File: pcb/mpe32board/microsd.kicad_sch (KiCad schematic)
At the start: 6 parts, among them J44 Micro_SD_Card

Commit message: layout stuff
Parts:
- J44: footprint (none) -> Connector_Card:microSD_HC_Molex_47219-2001
- R95, R96, R97, R98, R99: footprint (none) -> Resistor_SMD:R_0603_1608Metric
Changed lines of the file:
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@@
 			)
 		)
-		(property "Footprint" ""
+		(property "Footprint" "Resistor_SMD:R_0603_1608Metric"
 			(at 134.62 68.58 0)
 			(effects
@@
 			)
 		)
-		(property "Footprint" ""
+		(property "Footprint" "Resistor_SMD:R_0603_1608Metric"
 			(at 119.38 68.58 0)
 			(effects
@@
 			)
 		)
-		(property "Footprint" ""
+		(property "Footprint" "Connector_Card:microSD_HC_Molex_47219-2001"
 			(at 204.47 76.2 0)
 			(effects
@@
 			)
 		)
-		(property "Footprint" ""
+		(property "Footprint" "Resistor_SMD:R_0603_1608Metric"
 			(at 111.76 68.58 0)
 			(effects
@@
 			)
 		)
-		(property "Footprint" ""
+		(property "Footprint" "Resistor_SMD:R_0603_1608Metric"
 			(at 127 68.58 0)
 			(effects
@@
 			)
 		)
-		(property "Footprint" ""
+		(property "Footprint" "Resistor_SMD:R_0603_1608Metric"
 			(at 142.24 68.58 0)
 			(effects

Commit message: board layout stuff
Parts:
- removed J44: Micro_SD_Card, Connector_Card:microSD_HC_Molex_47219-2001, symbol Connector:Micro_SD_Card
- added J48: Micro_SD_Card_Det_Hirose_DM3AT, Connector_Card:microSD_HC_Hirose_DM3D-SF, symbol Connector:Micro_SD_Card_Det_Hirose_DM3AT
- added U11: IP4252CZ16, Package_SON:Nexperia_HUSON-16_USON-16-1EP_1.35x3.3mm_P0.4mm_EP0.4x2.8mm, symbol Power_Protection:IP4252CZ16
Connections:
- net +3V3: now also J48.4 (VDD)
- net GND: now also J48.11 (SHIELD), J48.6 (VSS), J48.9 (DET_B)
- net SDMMC1_CK: now also U11.6 (CH6)
- net SDMMC1_CMD: now also U11.4 (CH4)
- net SDMMC1_D0: now also U11.7 (CH7)
- net SDMMC1_D1: now also U11.8 (CH8)
- net SDMMC1_D2: now also U11.2 (CH2)
- net SDMMC1_D3: now also U11.3 (CH3)
- new net: J48.7 (DAT0), U11.10 (CH7)
- new net: J48.5 (CLK), U11.11 (CH6)
- new net: J48.3 (CMD), U11.13 (CH4)
- new net: J48.2 (DAT3/CD), U11.14 (CH3)
- new net: J48.1 (DAT2), U11.15 (CH2)
- new net: J48.10 (DET_A), U11.16 (CH1)
- new net: J48.8 (DAT1), U11.9 (CH8)
- new net SDCARD_DET: U11.1 (CH1)
- no-connect marks 0 -> 2
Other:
- note removed: "could use esd protection!!!"
- moved on the sheet: R95, R96, R97, R98, R99

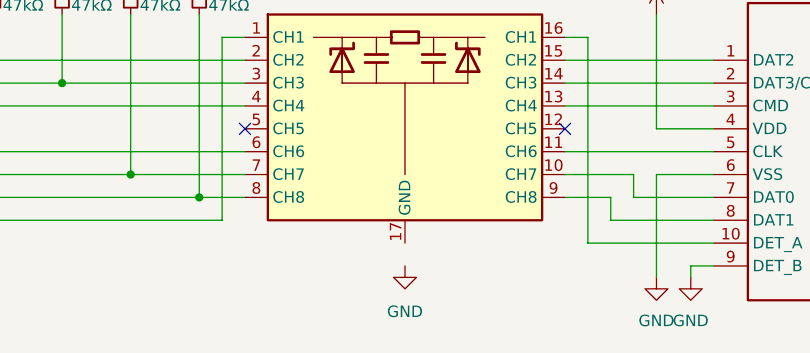
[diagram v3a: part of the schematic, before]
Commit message: routed audio codec and sdram
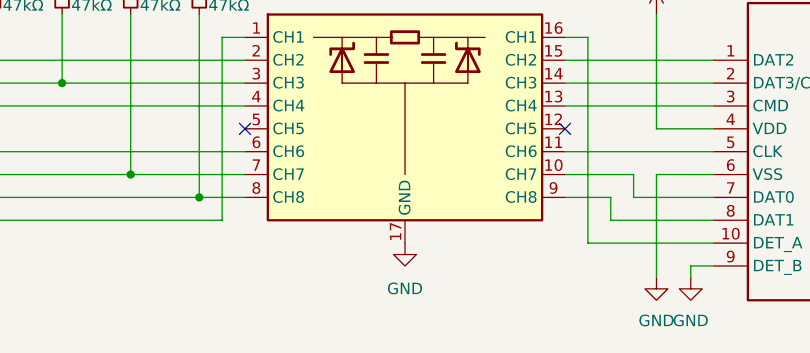
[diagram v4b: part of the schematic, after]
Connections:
- net GND: now also U11.17 (GND)
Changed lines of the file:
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@@
 	(symbol
 		(lib_id "power:GND")
-		(at 140.97 116.84 0)
+		(at 140.97 114.3 0)
 		(unit 1)
 		(body_style 1)
@@
 		(fields_autoplaced yes)
 		(property "Reference" "#PWR0172"
-			(at 140.97 123.19 0)
+			(at 140.97 120.65 0)
 			(hide yes)
 			(show_name no)
@@
 		)
 		(property "Value" "GND"
-			(at 140.97 121.92 0)
+			(at 140.97 119.38 0)
 			(show_name no)
 			(do_not_autoplace no)
@@
 		)
 		(property "Footprint" ""
-			(at 140.97 116.84 0)
+			(at 140.97 114.3 0)
 			(hide yes)
 			(show_name no)
@@
 		)
 		(property "Datasheet" ""
-			(at 140.97 116.84 0)
+			(at 140.97 114.3 0)
 			(hide yes)
 			(show_name no)
@@
 		)
 		(property "Description" "Power symbol creates a global label with name \"GND\" , ground"
-			(at 140.97 116.84 0)
+			(at 140.97 114.3 0)
 			(hide yes)
 			(show_name no)

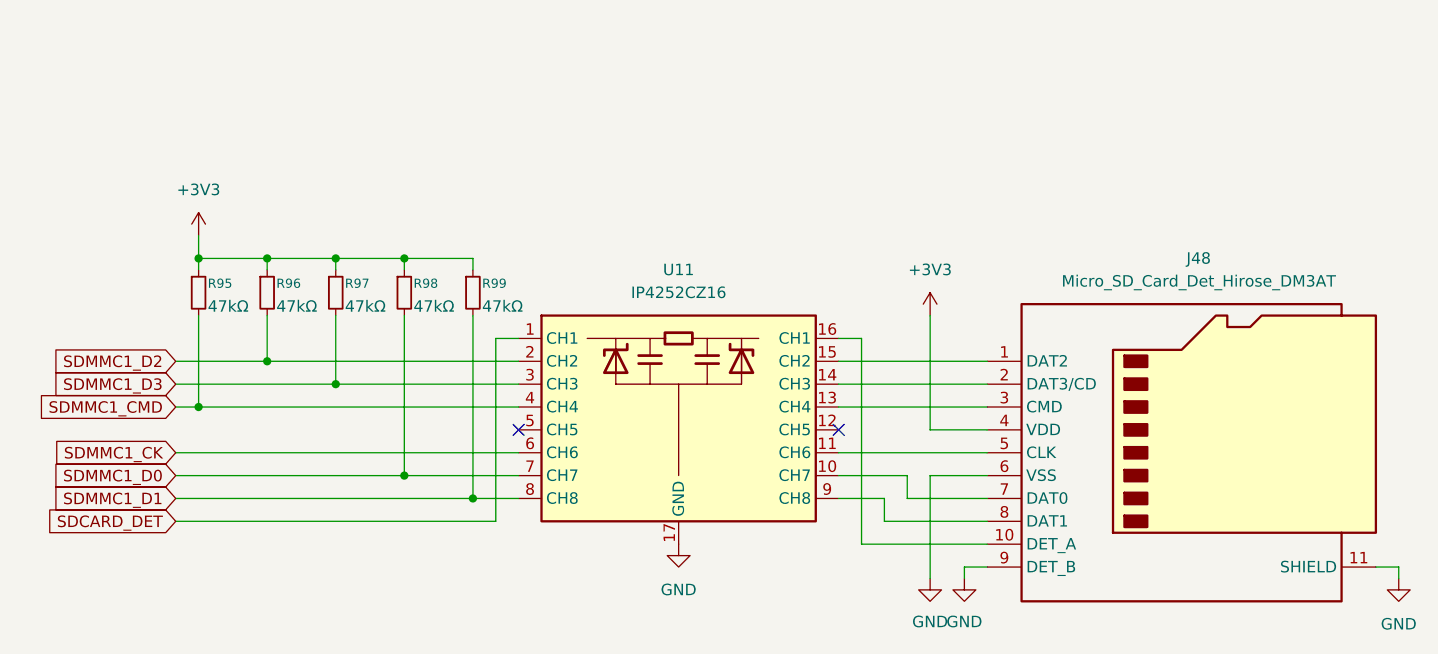
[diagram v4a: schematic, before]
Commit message: length match sdram
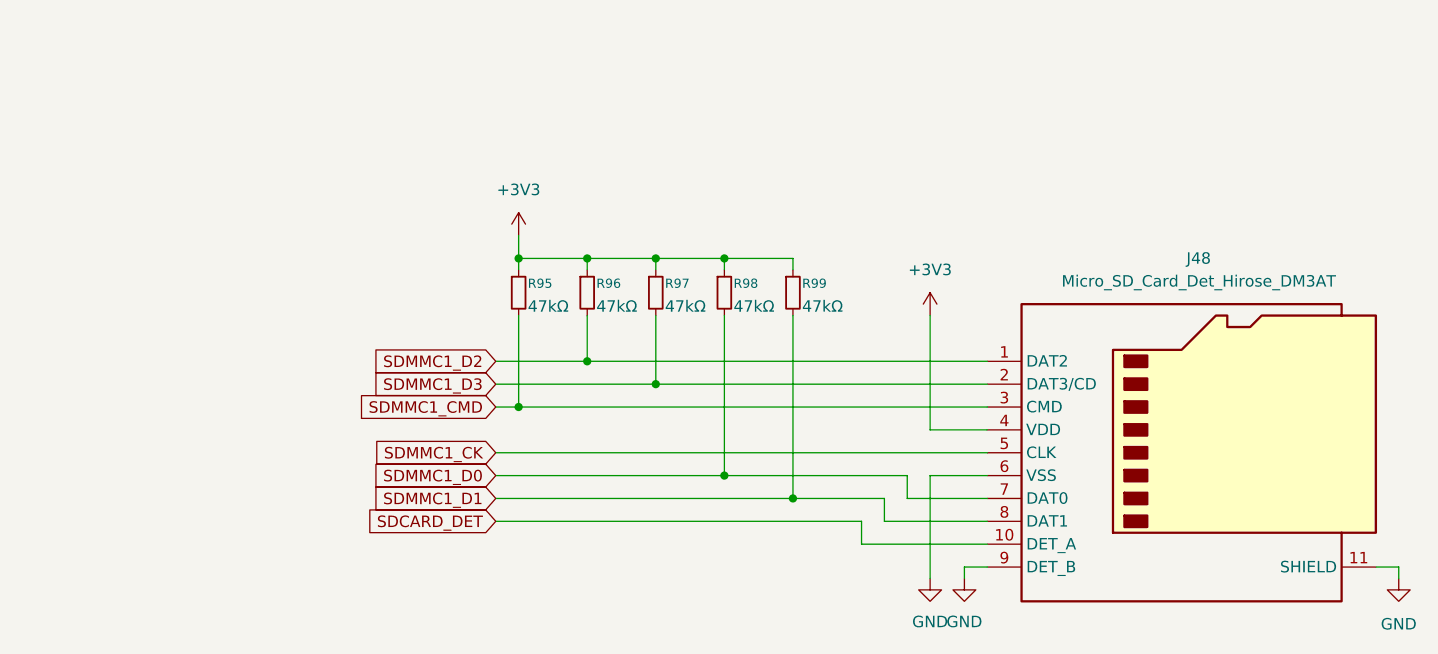
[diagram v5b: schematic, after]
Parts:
- removed U11: IP4252CZ16, Package_SON:Nexperia_HUSON-16_USON-16-1EP_1.35x3.3mm_P0.4mm_EP0.4x2.8mm, symbol Power_Protection:IP4252CZ16
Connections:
- net SDCARD_DET: now also J48.10 (DET_A)
- net SDMMC1_CK: now also J48.5 (CLK)
- net SDMMC1_CMD: now also J48.3 (CMD)
- net SDMMC1_D0: now also J48.7 (DAT0)
- net SDMMC1_D1: now also J48.8 (DAT1)
- net SDMMC1_D2: now also J48.1 (DAT2)
- net SDMMC1_D3: now also J48.2 (DAT3/CD)
- no-connect marks 2 -> 0
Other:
- moved on the sheet: R95, R96, R97, R98, R99

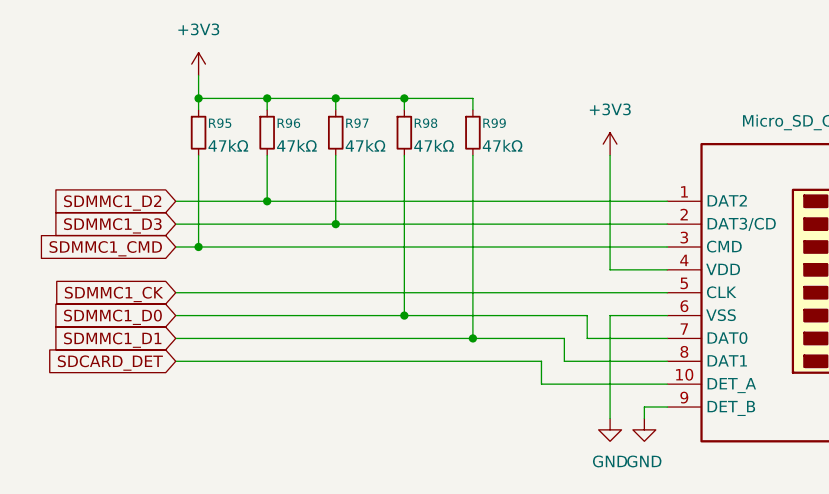
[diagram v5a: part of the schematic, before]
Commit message: add lcd level shifter, lm1117 ldo
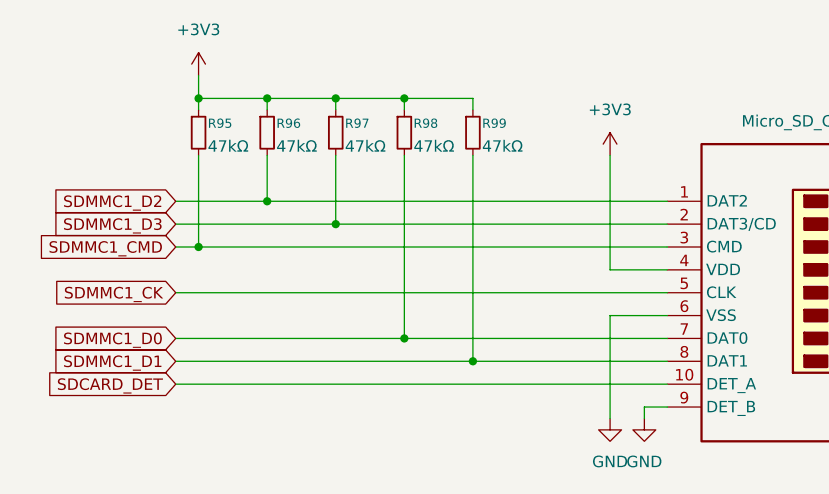
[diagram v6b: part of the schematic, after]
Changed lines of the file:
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@@
 	(paper "A4")
 	(junction
+		(at 153.67 111.76)
+		(diameter 0)
+		(color 0 0 0 0)
+	)
+	(junction
 		(at 138.43 82.55)
 		(diameter 0)
@@
 	)
 	(junction
+		(at 146.05 109.22)
+		(diameter 0)
+		(color 0 0 0 0)
+	)
+	(junction
 		(at 138.43 96.52)
 		(diameter 0)
@@
 	)
 	(junction
-		(at 146.05 106.68)
-		(diameter 0)
-		(color 0 0 0 0)
-	)
-	(junction
 		(at 123.19 99.06)
 		(diameter 0)
@@
 	)
 	(junction
-		(at 153.67 109.22)
-		(diameter 0)
-		(color 0 0 0 0)
-	)
-	(junction
 		(at 146.05 82.55)
 		(diameter 0)
@@
 	(wire
 		(pts
-			(xy 120.65 111.76) (xy 161.29 111.76)
-		)
-		(stroke
-			(width 0)
-			(type default)
-		)
-	)
-	(wire
-		(pts
-			(xy 120.65 109.22) (xy 153.67 109.22)
-		)
-		(stroke
-			(width 0)
-			(type default)
-		)
-	)
-	(wire
-		(pts
-			(xy 153.67 109.22) (xy 163.83 109.22)
+			(xy 120.65 114.3) (xy 175.26 114.3)
+		)
+		(stroke
+			(width 0)
+			(type default)
+		)
+	)
+	(wire
+		(pts
+			(xy 120.65 111.76) (xy 153.67 111.76)
+		)
+		(stroke
+			(width 0)
+			(type default)
+		)
+	)
+	(wire
+		(pts
+			(xy 153.67 111.76) (xy 175.26 111.76)
 		)
 		(stroke
@@
 	(wire
 		(pts
-			(xy 161.29 111.76) (xy 161.29 114.3)
-		)
-		(stroke
-			(width 0)
-			(type default)
-		)
-	)
-	(wire
-		(pts
 			(xy 153.67 82.55) (xy 153.67 83.82)
 		)
@@
 	(wire
 		(pts
-			(xy 120.65 106.68) (xy 146.05 106.68)
+			(xy 120.65 109.22) (xy 146.05 109.22)
 		)
 		(stroke
@@
 	(wire
 		(pts
-			(xy 163.83 109.22) (xy 163.83 111.76)
-		)
-		(stroke
-			(width 0)
-			(type default)
-		)
-	)
-	(wire
-		(pts
 			(xy 123.19 82.55) (xy 123.19 83.82)
 		)
@@
 	(wire
 		(pts
-			(xy 146.05 88.9) (xy 146.05 106.68)
-		)
-		(stroke
-			(width 0)
-			(type default)
-		)
-	)
-	(wire
-		(pts
 			(xy 120.65 93.98) (xy 130.81 93.98)
 		)
@@
 	(wire
 		(pts
+			(xy 153.67 88.9) (xy 153.67 111.76)
+		)
+		(stroke
+			(width 0)
+			(type default)
+		)
+	)
+	(wire
+		(pts
 			(xy 120.65 99.06) (xy 123.19 99.06)
 		)
@@
 	(wire
 		(pts
-			(xy 153.67 88.9) (xy 153.67 109.22)
-		)
-		(stroke
-			(width 0)
-			(type default)
-		)
-	)
-	(wire
-		(pts
-			(xy 163.83 111.76) (xy 175.26 111.76)
-		)
-		(stroke
-			(width 0)
-			(type default)
-		)
-	)
-	(wire
-		(pts
 			(xy 220.98 118.11) (xy 220.98 116.84)
 		)
@@
 	(wire
 		(pts
+			(xy 146.05 88.9) (xy 146.05 109.22)
+		)
+		(stroke
+			(width 0)
+			(type default)
+		)
+	)
+	(wire
+		(pts
 			(xy 123.19 82.55) (xy 130.81 82.55)
 		)
@@
 	(wire
 		(pts
-			(xy 146.05 106.68) (xy 166.37 106.68)
+			(xy 146.05 109.22) (xy 175.26 109.22)
 		)
 		(stroke
@@
 		)
 	)
-	(wire
-		(pts
-			(xy 161.29 114.3) (xy 175.26 114.3)
-		)
-		(stroke
-			(width 0)
-			(type default)
-		)
-	)
-	(wire
-		(pts
-			(xy 166.37 109.22) (xy 175.26 109.22)
-		)
-		(stroke
-			(width 0)
-			(type default)
-		)
-	)
-	(wire
-		(pts
-			(xy 166.37 106.68) (xy 166.37 109.22)
-		)
-		(stroke
-			(width 0)
-			(type default)
-		)
-	)
 	(global_label "SDCARD_DET"
 		(shape input)
-		(at 120.65 111.76 180)
-		(fields_autoplaced yes)
-		(effects
-			(font
-				(size 1.27 1.27)
-			)
-			(justify right)
-		)
-		(property "Intersheetrefs" "${INTERSHEET_REFS}"
-			(at 105.9325 111.76 0)
+		(at 120.65 114.3 180)
+		(fields_autoplaced yes)
+		(effects
+			(font
+				(size 1.27 1.27)
+			)
+			(justify right)
+		)
+		(property "Intersheetrefs" "${INTERSHEET_REFS}"
+			(at 105.9325 114.3 0)
 			(hide yes)
 			(show_name no)
@@
 	(global_label "SDMMC1_D0"
 		(shape input)
-		(at 120.65 106.68 180)
-		(fields_autoplaced yes)
-		(effects
-			(font
-				(size 1.27 1.27)
-			)
-			(justify right)
-		)
-		(property "Intersheetrefs" "${INTERSHEET_REFS}"
-			(at 106.3559 106.68 0)
+		(at 120.65 109.22 180)
+		(fields_autoplaced yes)
+		(effects
+			(font
+				(size 1.27 1.27)
+			)
+			(justify right)
+		)
+		(property "Intersheetrefs" "${INTERSHEET_REFS}"
+			(at 106.3559 109.22 0)
 			(hide yes)
 			(show_name no)
@@
 	(global_label "SDMMC1_D1"
 		(shape input)
-		(at 120.65 109.22 180)
-		(fields_autoplaced yes)
-		(effects
-			(font
-				(size 1.27 1.27)
-			)
-			(justify right)
-		)
-		(property "Intersheetrefs" "${INTERSHEET_REFS}"
-			(at 106.3559 109.22 0)
-			(hide yes)
-			(show_name no)
+		(at 120.65 111.76 180)
+		(fields_autoplaced yes)
+		(effects
+			(font
+				(size 1.27 1.27)
+			)
+			(justify right)
+		)
+		(property "Intersheetrefs" "${INTERSHEET_REFS}"
+			(at 106.3559 111.76 0)
+			(hide yes)
+			(show_name no)
